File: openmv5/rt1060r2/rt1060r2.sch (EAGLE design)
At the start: 235 parts, among them CN1 S2B-PH-K-S(LF)(SN), IC1 LM66200DRLR, IC10 TCR2LF33,LM_CT, IC2 AP61300Z6-7, IC3 IS42S16160G-6BL, IC4 ATECC608B-MAHDA-T, IC5 IS25LP064D-JKLE-TR, IC7 MXC4005XC, IC8 MIMXRT1052DVL6B, IC9 KSZ8081RNDCA-TR, J1 USB4105-GF-A, J2 DNP, J3 DNP, J4 DF12-36-DS, J5 USD-1040310811, J6 DNP, J7 DNP, J8 3221-10-0300-00, M1 9774030151R, M2 9774030151R, Q1 2N7002KW_R1_00001, Q2 2N7002KW_R1_00001, Q3 2N7002KW_R1_00001, Q4 2N7002KW_R1_00001, Q5 2N7002KW_R1_00001, Q6 DMG2301L-7, Q7 2N7002KW_R1_00001, U2 BQ24075RGTR, U3 LBEE5KL1DX-883, Y1 SC32S-7PF20PPM, Y2 XRCGB24M000F3M00R0, Y3 ECS-327MVATX-3-CN-TR3

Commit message: Update R2 board per all feedback so far
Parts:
- removed C111: 0.1uF, 0402:CAP_0402
- removed IC10: TCR2LF33,LM_CT, TCR2LF33_LM_CT:TCR2LF33,LM_CT
- removed L9: MAKK2016T2R2M, MAKK2016T2R2M:MAKK2016T2R2M
- removed U3: LBEE5KL1DX-883, LBEE5KL1DX-TEMP:LBEE5KL1DX-TEMP
- added C24: 0.22uF, rcl:C-EUC0201
- added C25: 4.7uF, 0402:CAP_0402
- added D11, D12, D13, D14: CPDQT5V0HE-HF, CPDQT5V0HE-HF:CPDQT5V0HE-HF
- added D15: RB521S30T5G, RB521S30T5G:RB521S30T5G
- added IC6: ATECC608B-MAHDA-T, ATECC608B-MAHDA-T:ATECC608B-MAHDA-T
- added J9: DNP, 2337019-1:2337019-1
- added L3: 100, 0402:INDUCTOR_0402
- added R60, R61, R63: 10K, 0402:RES_0402
- added R62: 2.2M, 0402:RES_0402
- added TP1, TP2: TPTP10R, testpad:TPTP10R
- added U1: BQ24075RGTR, BQ24075RGTR:BQ24075RGTR
- C1: value 4.7uF -> 1nF; device sfe:CAP0402-CAP -> 0402:CAP_0402; MPN JMK105BBJ475MV-F -> VJ0402Y102JXACW1BC
- C10, C40, C65, C81: value 4.7uF -> 22uF; device sfe:CAP0402-CAP -> SparkFun-Capacitors:22UF-0805-6.3V-20%; MPN JMK105BBJ475MV-F -> CL21A226MQQNNNE
- C101, C2, C23, C27, C3, C35, C39, C4, C41, C42, C44, C5, C57, C72, C8, C9, C92: device sfe:CAP0402-CAP -> 0402:CAP_0402
- C103, C13, C28, C31, C38, C43, C48, C59, C62, C66, C98: value 0.22uF -> 4.7uF; device rcl:C-EUC0201 -> 0402:CAP_0402; MPN GRM033R60J224ME15D -> JMK105BBJ475MV-F
- C104, C12, C17, C21, C60, C64, C67, C83, C90, C91, C93, C95: value 4.7uF -> 0.22uF; device sfe:CAP0402-CAP -> rcl:C-EUC0201; MPN JMK105BBJ475MV-F -> GRM033R60J224ME15D
- C107: value 0.22uF -> 18pF; MPN GRM033R60J224ME15D -> GRM0335C1E180JA01D
- C108: value 4.7uF -> 18pF; device sfe:CAP0402-CAP -> rcl:C-EUC0201; MPN JMK105BBJ475MV-F -> GRM0335C1E180JA01D
- C11, C15, C19, C34, C45: value 0.22uF -> 22uF; device rcl:C-EUC0201 -> SparkFun-Capacitors:22UF-0805-6.3V-20%; MPN GRM033R60J224ME15D -> CL21A226MQQNNNE
- C110: value 1nF -> 4.7uF; device sfe:CAP0402-CAP -> 0402:CAP_0402; MPN VJ0402Y102JXACW1BC -> JMK105BBJ475MV-F
- C14, C61, C73, C85, C96: value 22uF -> 0.22uF; device SparkFun-Capacitors:22UF-0805-6.3V-20% -> rcl:C-EUC0201; MPN CL21A226MQQNNNE -> GRM033R60J224ME15D
- C18, C37, C58, C6, C7: value 22uF -> 4.7uF; device SparkFun-Capacitors:22UF-0805-6.3V-20% -> 0402:CAP_0402; MPN CL21A226MQQNNNE -> JMK105BBJ475MV-F
- C20: value 1uF -> 0.22uF; device 0402:CAP_0402 -> rcl:C-EUC0201; MPN C0402C104Z4VAC -> GRM033R60J224ME15D
- C22, C74: value 0.1uF -> 22uF; device 0402:CAP_0402 -> SparkFun-Capacitors:22UF-0805-6.3V-20%; MPN C0402C104Z4VAC -> CL21A226MQQNNNE
- C29: value 22uF -> 1uF; device SparkFun-Capacitors:22UF-0805-6.3V-20% -> 0402:CAP_0402; MPN CL21A226MQQNNNE -> C0402C104Z4VAC
- C30, C33, C46: value 4.7uF -> 0.1uF; device sfe:CAP0402-CAP -> 0402:CAP_0402; MPN JMK105BBJ475MV-F -> C0402C104Z4VAC
- C36, C82, C84: value 0.1uF -> 4.7uF; MPN C0402C104Z4VAC -> JMK105BBJ475MV-F
- C47, C50, C54, C55, C56: value 0.22uF -> 0.1uF; device rcl:C-EUC0201 -> 0402:CAP_0402; MPN GRM033R60J224ME15D -> C0402C104Z4VAC
- C51: value 22uF -> 0.1uF; device SparkFun-Capacitors:22UF-0805-6.3V-20% -> 0402:CAP_0402; MPN CL21A226MQQNNNE -> C0402C104Z4VAC
- C52: value 4.7uF -> GRM0335C1H1R5BA01D; device sfe:CAP0402-CAP -> GRM0335C1H1R5BA01D:GRM0335C1H1R5BA01D; MPN JMK105BBJ475MV-F -> GRM0335C1H1R5BA01D
- C53: value 0.22uF -> DNP; device rcl:C-EUC0201 -> GRM0335C1H1R5BA01D:GRM0335C1H1R5BA01D; MPN GRM033R60J224ME15D -> GRM0335C1H1R5BA01D; POPULATE (none) -> 0
- C75, C76, C89: value 0.1uF -> 0.22uF; device 0402:CAP_0402 -> rcl:C-EUC0201; MPN C0402C104Z4VAC -> GRM033R60J224ME15D
- C77: value GRM0335C1H1R5BA01D -> 4.7uF; device GRM0335C1H1R5BA01D:GRM0335C1H1R5BA01D -> 0402:CAP_0402; MPN GRM0335C1H1R5BA01D -> JMK105BBJ475MV-F
- C78: value DNP -> 22uF; device GRM0335C1H1R5BA01D:GRM0335C1H1R5BA01D -> SparkFun-Capacitors:22UF-0805-6.3V-20%; MPN GRM0335C1H1R5BA01D -> CL21A226MQQNNNE; POPULATE 0 -> (none)
- C79: value 18pF -> 4.7uF; device rcl:C-EUC0201 -> 0402:CAP_0402; MPN GRM0335C1E180JA01D -> JMK105BBJ475MV-F
- C80: value 18pF -> 0.22uF; MPN GRM0335C1E180JA01D -> GRM033R60J224ME15D
- D3: value UHD1110-FKA-CL1A13R3Q1BBQFMF3 -> RB521S30T5G; device UHD1110-FKA-CL1A13R3Q1BBQFMF3:UHD1110-FKA-CL1A13R3Q1BBQFMF3 -> RB521S30T5G:RB521S30T5G; MPN UHD1110-FKA-CL1A13r3q1BBQFMF3 -> RB521S30T5G
- D4: value CPDQT5V0HE-HF -> RB521S30T5G; device CPDQT5V0HE-HF:CPDQT5V0HE-HF -> RB521S30T5G:RB521S30T5G; MPN CPDQT5V0HE-HF -> RB521S30T5G
- D5: value CPDQT5V0HE-HF -> UHD1110-FKA-CL1A13R3Q1BBQFMF3; device CPDQT5V0HE-HF:CPDQT5V0HE-HF -> UHD1110-FKA-CL1A13R3Q1BBQFMF3:UHD1110-FKA-CL1A13R3Q1BBQFMF3; MPN CPDQT5V0HE-HF -> UHD1110-FKA-CL1A13r3q1BBQFMF3
- IC2: value AP61300Z6-7 -> TCR2LF33,LM_CT; device AP61300Z6-7:AP61300Z6-7 -> TCR2LF33_LM_CT:TCR2LF33,LM_CT; MPN AP61300Z6-7 -> TCR2LF33,LM(CT
- IC3: value IS42S16160G-6BL -> AP61300Z6-7; device IS42S16160G-6BL:IS42S16160G-6BL -> AP61300Z6-7:AP61300Z6-7; MPN IS42S16160G-6BL -> AP61300Z6-7
- IC4: value ATECC608B-MAHDA-T -> IS42S16160G-6BL; device ATECC608B-MAHDA-T:ATECC608B-MAHDA-T -> IS42S16160G-6BL:IS42S16160G-6BL; MPN ATECC608B-MAHDA-T -> IS42S16160G-6BL
- IC5: value IS25LP064D-JKLE-TR -> IS25LP128F-JKLE-TR; DESCRIPTION (none) -> NOR Flash 128M 2.3-3.6V 166Mhz Serial NOR Flash; MANUFACTURER_PART_NUMBER (none) -> IS25LP128F-JKLE-TR; MOUSER_PART_NUMBER (none) -> 870-5LP128F-JKLE-TR; MOUSER_PRICE-STOCK (none) -> https://www.mouser.com/ProductDetail/ISSI/IS25LP128F-JKLE-T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; MPN IS25LP064D-JKLE-TR -> IS25LP128F-JKLE-TR
- IC8: value MIMXRT1052DVL6B -> KSZ8081RNDCA-TR; device MIMXRT1052DVL6B:MIMXRT1052DVL6B -> KSZ8081RNDCA-TR:KSZ8081RNDCA-TR; MPN MIMXRT1052DVL6B -> KSZ8081RNDCA-TR
- IC9: value KSZ8081RNDCA-TR -> MIMXRT1052DVL6B; device KSZ8081RNDCA-TR:KSZ8081RNDCA-TR -> MIMXRT1052DVL6B:MIMXRT1052DVL6B; MPN KSZ8081RNDCA-TR -> MIMXRT1052DVL6B
- J2: value DNP -> USD-1040310811; device SparkFun-Connectors:CONN_08" -> 1040310811:USD-1040310811; MPN (none) -> 104031-0811; POPULATE 0 -> (none)
- J3: value DNP -> DF12-36-DS; device SparkFun-Connectors:CONN_08" -> DF12-36-DS:DF12-36-DS; MPN (none) -> DF12NB(3.0)-36DS-0.5V(51); POPULATE 0 -> (none)
- J4: value DF12-36-DS -> DNP; device DF12-36-DS:DF12-36-DS -> SparkFun-Connectors:CONN_08"; MPN DF12NB(3.0)-36DS-0.5V(51) -> (none); POPULATE (none) -> 0
- J5: value USD-1040310811 -> DNP; device 1040310811:USD-1040310811 -> SparkFun-Connectors:CONN_08"; MPN 104031-0811 -> (none); POPULATE (none) -> 0
- J7: device 2337019-1:2337019-1 -> SparkFun-Connectors:CONN_08"; MPN 2337019-1 -> (none)
- L4, L8: device sfe:INDUCTOR0402 -> 0402:INDUCTOR_0402
- L5: value MAKK2016T4R7M -> 3.9NH; device MAKK2016T4R7M:MAKK2016T4R7M -> SparkFun-Coils:INDUCTOR-0402-3.9NH; MPN MAKK2016T4R7M -> L-07C3N9SV6T
- L6: value 100 -> MAKK2016T2R2M; device sfe:INDUCTOR0402 -> MAKK2016T2R2M:MAKK2016T2R2M; MPN MFBM1V1005-101-R -> MAKK2016T2R2M
- L7: value 3.9NH -> MAKK2016T4R7M; device SparkFun-Coils:INDUCTOR-0402-3.9NH -> MAKK2016T4R7M:MAKK2016T4R7M; MPN L-07C3N9SV6T -> MAKK2016T4R7M
- Q1: value 2N7002KW_R1_00001 -> DMG2301L-7; device 2N7002KW_R1_00001:2N7002KW_R1_00001 -> DMG2301L-7:DMG2301L-7; MPN 2N7002KW_R1_00001 -> DMG2301L-7
- Q6: value DMG2301L-7 -> 2N7002KW_R1_00001; device DMG2301L-7:DMG2301L-7 -> 2N7002KW_R1_00001:2N7002KW_R1_00001; MPN DMG2301L-7 -> 2N7002KW_R1_00001
- R1, R5: value 1K -> 5.1K; device sfe:RESISTOR0402-RES -> 0402:RES_0402; MPN CRCW04021K00FKEDC -> RC0402JR-075K1L
- R10: value 1.1K -> 8.2K; device sfe:RESISTOR0402-RES -> 0402:RES_0402; MPN RC0402JR-071K1L -> CR0402-FX-8201GLF
- R11: value 46.4K -> 100K; device sfe:RESISTOR0402-RES -> 0402:RES_0402; MPN WR04X4642FTL -> AC0402FR-07100KL
- R12: value 8.2K -> 100K; device sfe:RESISTOR0402-RES -> 0402:RES_0402; MPN CR0402-FX-8201GLF -> AC0402FR-07100KL
- R13, R18, R34, R36, R4: device sfe:RESISTOR0402-RES -> 0402:RES_0402
- R15: value 2.7K -> 200K; device sfe:RESISTOR0402-RES -> 0402:RES_0402; MPN AC0402JR-072K7L -> CRCW0402200KFKEDC
- R16: value 2.7K -> 100K; device sfe:RESISTOR0402-RES -> 0402:RES_0402; MPN AC0402JR-072K7L -> AC0402FR-07100KL
- R17: value 2.7K -> 44.2K; device sfe:RESISTOR0402-RES -> 0402:RES_0402; MPN AC0402JR-072K7L -> AC0402FR-0744K2L
- R19, R35: value 220 -> 100K; device sfe:RESISTOR0402-RES -> 0402:RES_0402; MPN CRGCQ0402F220R -> AC0402FR-07100KL
- R2: value 200K -> 5.1K; device sfe:RESISTOR0402-RES -> 0402:RES_0402; MPN CRCW0402200KFKEDC -> RC0402JR-075K1L
- R20: value 220 -> 1K; device sfe:RESISTOR0402-RES -> 0402:RES_0402; MPN CRGCQ0402F220R -> CRCW04021K00FKEDC
- R21: value 220 -> 10K; device sfe:RESISTOR0402-RES -> 0402:RES_0402; MPN CRGCQ0402F220R -> AC0402FR-1310KL
- R22: value 100K -> 5.1K; device sfe:RESISTOR0402-RES -> 0402:RES_0402; MPN AC0402FR-07100KL -> RC0402JR-075K1L
- R23, R24, R25: value 100K -> 10K; device sfe:RESISTOR0402-RES -> 0402:RES_0402; MPN AC0402FR-07100KL -> AC0402FR-1310KL
- R26: value 1K -> 2.7K; device sfe:RESISTOR0402-RES -> 0402:RES_0402; MPN CRCW04021K00FKEDC -> AC0402JR-072K7L
- R27: value 10K -> 2.7K; device sfe:RESISTOR0402-RES -> 0402:RES_0402; MPN AC0402FR-1310KL -> AC0402JR-072K7L
- R28: value 100K -> 2.7K; device sfe:RESISTOR0402-RES -> 0402:RES_0402; MPN AC0402FR-07100KL -> AC0402JR-072K7L
- R29, R33, R37: value 10K -> 100K; device sfe:RESISTOR0402-RES -> 0402:RES_0402; MPN AC0402FR-1310KL -> AC0402FR-07100KL
- R3: value 100K -> 1M; device sfe:RESISTOR0402-RES -> 0402:RES_0402; MPN AC0402FR-07100KL -> CRCW04021M00FKEDC
- R30, R31: value 4.7K -> 100K; device sfe:RESISTOR0402-RES -> 0402:RES_0402; MPN AC0402FR-074K7L -> AC0402FR-07100KL
- R32: value 30K -> 100K; device sfe:RESISTOR0402-RES -> 0402:RES_0402; MPN 0402WGF3002TCE -> AC0402FR-07100KL
- R38: value 6.49K -> 10K; device sfe:RESISTOR0402-RES -> 0402:RES_0402; MPN CR0402-FX-6491GLF -> AC0402FR-1310KL
- R39: value 1K -> 100K; device sfe:RESISTOR0402-RES -> 0402:RES_0402; MPN CRCW04021K00FKEDC -> AC0402FR-07100KL
- R40: value 2.2M -> 10K; device sfe:RESISTOR0402-RES -> 0402:RES_0402; MPN RC0402FR-072M2L -> AC0402FR-1310KL
- R41: value 1M -> 4.7K; device sfe:RESISTOR0402-RES -> 0402:RES_0402; MPN CRCW04021M00FKEDC -> AC0402FR-074K7L
- R42: value 10K -> 4.7K; device sfe:RESISTOR0402-RES -> 0402:RES_0402; MPN AC0402FR-1310KL -> AC0402FR-074K7L
- R45, R46: value 100K -> DNP; MPN AC0402FR-07100KL -> DNP
- R48: value 100K -> 220; MPN AC0402FR-07100KL -> CRGCQ0402F220R
- R49, R51: value 100K -> 1K; MPN AC0402FR-07100KL -> CRCW04021K00FKEDC
- R50: value 100K -> 6.49K; MPN AC0402FR-07100KL -> CR0402-FX-6491GLF
- R52, R53: value 100K -> 10K; MPN AC0402FR-07100KL -> AC0402FR-1310KL
- R56, R57, R58: value 10K -> 100K; MPN AC0402FR-1310KL -> AC0402FR-07100KL
- R59: value 100K -> 30K; MPN AC0402FR-07100KL -> 0402WGF3002TCE
- R6, R7: value 5.1K -> 10K; device sfe:RESISTOR0402-RES -> 0402:RES_0402; MPN RC0402JR-075K1L -> AC0402FR-1310KL
- R8: value 44.2K -> 1.1K; device sfe:RESISTOR0402-RES -> 0402:RES_0402; MPN AC0402FR-0744K2L -> RC0402JR-071K1L
- R9: value 10K -> 46.4K; device sfe:RESISTOR0402-RES -> 0402:RES_0402; MPN AC0402FR-1310KL -> WR04X4642FTL
- U2: value BQ24075RGTR -> LBEE5KL1DX-883; device BQ24075RGTR:BQ24075RGTR -> LBEE5KL1DX-TEMP:LBEE5KL1DX-TEMP; MPN BQ24075RGTR -> LBEE5KL1DX-883
- Y1: value SC32S-7PF20PPM -> ECS-327MVATX-3-CN-TR3; device ABS07-32.768KHZ-7-T:ABS07-32.768KHZ-7-T -> ECS-327MVATX-3-CN-TR3:ECS-327MVATX-3-CN-TR3; MPN SC32S-7PF20PPM -> ECS-327MVATX-3-CN-TR3
- Y3: value ECS-327MVATX-3-CN-TR3 -> SC32S-7PF20PPM; device ECS-327MVATX-3-CN-TR3:ECS-327MVATX-3-CN-TR3 -> ABS07-32.768KHZ-7-T:ABS07-32.768KHZ-7-T; MPN ECS-327MVATX-3-CN-TR3 -> SC32S-7PF20PPM
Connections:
- removed net SBL_BOOT: R42.2, S1.COM_1, S1.COM_2, S1.COM_3
- new net JTAG_TDI_INT_UNUSED: J8.8, R45.2
- new net JTAG_TRSTB_INT_UNUSED: J8.9, R46.2
- new net PMIC_STBY_REQ: C110.2, D15.K, IC9.PMIC_STBY_REQ, R63.1
- new net SBL: D13.1, J6.2, R43.2
- new net SNVS_BAT: D4.A, TP1.TP
- new net SWITCH: D15.A, R61.1, R63.2, S1.COM_1, S1.COM_2, S1.COM_3
- new net VDD_SNVS_CPU: C86.1, D3.K, D4.K, IC9.VDD_SNVS_IN
- net ANT: now also C52.1, J9.SIGNAL, L5.2, U2.ANT; no longer C77.1, J7.SIGNAL, L7.2, U3.ANT
- net BAT: now also C5.2, U1.BAT_2, U1.BAT_3; no longer C8.2, U2.BAT_2, U2.BAT_3
- net BT_D_WAKE: now also IC9.GPIO_SD_B1_00, U2.BT_DEV_WAKE; no longer IC8.GPIO_SD_B1_00, U3.BT_DEV_WAKE
- net BT_H_WAKE: now also IC9.GPIO_AD_B0_14, R53.1, U2.BT_HOST_WAKE; no longer IC8.GPIO_AD_B0_14, R44.1, U3.BT_HOST_WAKE
- net BT_REG_ON: now also IC9.GPIO_AD_B0_08, R44.1, U2.BT_REG_ON; no longer IC8.GPIO_AD_B0_08, R37.1, U3.BT_REG_ON
- net BT_UART_CTS: now also IC9.GPIO_AD_B1_04, U2.!BT_UART_RTS_N; no longer IC8.GPIO_AD_B1_04, U3.!BT_UART_RTS_N
- net BT_UART_RTS: now also IC9.GPIO_AD_B1_05, U2.!BT_UART_CTS_N; no longer IC8.GPIO_AD_B1_05, U3.!BT_UART_CTS_N
- net BT_UART_RX: now also IC9.GPIO_B0_09, U2.BT_UART_TXD; no longer IC8.GPIO_B0_09, U3.BT_UART_TXD
- net BT_UART_TX: now also IC9.GPIO_B0_08, U2.BT_UART_RXD; no longer IC8.GPIO_B0_08, U3.BT_UART_RXD
- net CC1: now also R1.1; no longer R6.1
- net CC2: now also R2.1; no longer R7.1
- net CHG: now also R5.1, U1.!CHG; no longer R1.1, U2.!CHG
- net DCDC_LP: now also IC9.DCDC_LP_1, IC9.DCDC_LP_2, L7.2; no longer IC8.DCDC_LP_1, IC8.DCDC_LP_2, L5.2
- net DCDC_PSWITCH: now also C96.1, IC9.DCDC_PSWITCH, R59.1; no longer C62.1, IC8.DCDC_PSWITCH, R32.1
- net DCMI_CLK: now also IC9.GPIO_B1_15, J3.12; no longer IC8.GPIO_B1_15, J4.12
- net DCMI_D0: now also IC9.GPIO_AD_B1_15, J3.31; no longer IC8.GPIO_AD_B1_15, J4.31
- net DCMI_D1: now also IC9.GPIO_AD_B1_14, J3.29; no longer IC8.GPIO_AD_B1_14, J4.29
- net DCMI_D2: now also IC9.GPIO_AD_B1_13, J3.35; no longer IC8.GPIO_AD_B1_13, J4.35
- net DCMI_D3: now also IC9.GPIO_AD_B1_12, J3.28; no longer IC8.GPIO_AD_B1_12, J4.28
- net DCMI_D4: now also IC9.GPIO_AD_B1_11, J3.26; no longer IC8.GPIO_AD_B1_11, J4.26
- net DCMI_D5: now also IC9.GPIO_AD_B1_10, J3.33; no longer IC8.GPIO_AD_B1_10, J4.33
- net DCMI_D6: now also IC9.GPIO_AD_B0_05, J3.24; no longer IC8.GPIO_AD_B0_05, J4.24
- net DCMI_D7: now also IC9.GPIO_AD_B0_04, J3.22, R43.1; no longer IC8.GPIO_AD_B0_04, J4.22, S1.NO_1, S1.NO_2
- net DCMI_FSIN: now also J3.23, Q7.D, R39.1; no longer J4.23, Q5.D, R28.1
- net DCMI_HSYNC: now also IC9.GPIO_AD_B0_15, J3.18; no longer IC8.GPIO_AD_B0_15, J4.18
- net DCMI_MISO: now also IC9.GPIO_B0_01, J3.15; no longer IC8.GPIO_B0_01, J4.15
- net DCMI_MOSI: now also IC9.GPIO_B0_02, J3.17; no longer IC8.GPIO_B0_02, J4.17
- net DCMI_PCLK: now also IC9.GPIO_B1_12, J3.14; no longer IC8.GPIO_B1_12, J4.14
- net DCMI_PWDN: now also IC9.GPIO_B1_02, J3.25, R40.1; no longer IC8.GPIO_B1_02, J4.25, R29.1
- net DCMI_RST: now also IC9.GPIO_B1_01, J3.21, R38.1; no longer IC8.GPIO_B1_01, J4.21, R27.1
- net DCMI_SCL: now also IC9.GPIO_AD_B1_00, J3.32, R41.1; no longer IC8.GPIO_AD_B1_00, J4.32, R30.1
- net DCMI_SCLK: now also IC9.GPIO_B0_03, J3.13; no longer IC8.GPIO_B0_03, J4.13
- net DCMI_SDA: now also IC9.GPIO_AD_B1_01, J3.34, R42.1; no longer IC8.GPIO_AD_B1_01, J4.34, R31.1
- net DCMI_SSEL: now also IC9.GPIO_B0_00, J3.11, R37.1; no longer IC8.GPIO_B0_00, J4.11, R24.1
- net DCMI_VSYNC: now also IC9.GPIO_B1_13, J3.16; no longer IC8.GPIO_B1_13, J4.16
- net EN: now also IC3.EN, Q5.D, R16.1; no longer IC2.EN, Q1.D, R3.1
- net ETH_INT: now also IC8.INTRP, IC9.GPIO_B0_12, R49.1; no longer IC8.GPIO_B0_12, IC9.INTRP, R36.1
- net ETH_LED: now also IC8.LED0_/_ANEN_SPEED, R48.1; no longer IC9.LED0_/_ANEN_SPEED, R35.1
- net ETH_MDC: now also IC8.MDC, IC9.GPIO_EMC_40; no longer IC8.GPIO_EMC_40, IC9.MDC
- net ETH_MDIO: now also IC8.MDIO, IC9.GPIO_EMC_41, R51.1; no longer IC8.GPIO_EMC_41, IC9.MDIO, R39.1
- net ETH_RST: now also C42.2, IC8.RST#, IC9.GPIO_B0_13, R47.1; no longer C65.2, IC8.GPIO_B0_13, IC9.RST#, R34.1
- net ETH_RXD0: now also IC8.RXD0, IC9.GPIO_B1_04; no longer IC8.GPIO_B1_04, IC9.RXD0
- net ETH_RXD1: now also IC8.RXD1, IC9.GPIO_B1_05; no longer IC8.GPIO_B1_05, IC9.RXD1
- net ETH_RXDV: now also IC8.CRS_DV/_PHYAD[1:0], IC9.GPIO_B1_06; no longer IC8.GPIO_B1_06, IC9.CRS_DV/_PHYAD[1:0]
- net ETH_RXERR: now also IC8.RXER, IC9.GPIO_B1_11; no longer IC8.GPIO_B1_11, IC9.RXER
- net ETH_TXCLK: now also IC8.XI, IC9.GPIO_B1_10; no longer IC8.GPIO_B1_10, IC9.XI
- net ETH_TXD0: now also IC8.TXD0, IC9.GPIO_B1_07; no longer IC8.GPIO_B1_07, IC9.TXD0
- net ETH_TXD1: now also IC8.TXD1, IC9.GPIO_B1_08; no longer IC8.GPIO_B1_08, IC9.TXD1
- net ETH_TXEN: now also IC8.TXEN, IC9.GPIO_B1_09; no longer IC8.GPIO_B1_09, IC9.TXEN
- net ETH_VDDA_3.3: now also C43.2, C45.1, C46.1, IC8.VDDA_3.3, L4.P$1; no longer C81.2, C82.1, C85.1, IC9.VDDA_3.3, L8.1
- net ETH_VDD_1.2: now also C44.2, C47.1, IC8.VDD_1.2; no longer C83.2, C84.1, IC9.VDD_1.2
- net FB: now also IC3.FB, R15.1, R17.2; no longer IC2.FB, R2.1, R8.2
- net FEED: now also C53.1, L5.1; no longer C78.1, L7.1
- net GND: now also C10.2, C104.2, C108.2, C11.2, C12.1, C17.2, C19.1, C21.2, C23.2, C24.1, C25.1, C28.1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; no longer C10.1, C104.1, C108.1, C11.1, C111.2, C12.2, C17.1, C19.2, C21.1, C23.1, C28.2, C33.1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
- net ILIM: now also R8.1, U1.ILIM; no longer R10.1, U2.ILIM
- net INT_I2C_INT: now also IC9.GPIO_B1_03, R28.1; no longer IC8.GPIO_B1_03, R17.1
- net INT_I2C_SCL: now also IC6.SCL, IC9.GPIO_B0_04, R26.1; no longer IC4.SCL, IC8.GPIO_B0_04, R15.1
- net INT_I2C_SDA: now also IC6.SDA, IC9.GPIO_B0_05, R27.1; no longer IC4.SDA, IC8.GPIO_B0_05, R16.1
- net ISET: now also R10.1, U1.ISET; no longer R12.1, U2.ISET
- net JTAG_TCK: now also FL5.INPUT_5, IC9.GPIO_AD_B0_07; no longer FL5.INPUT_4, IC8.GPIO_AD_B0_07
- net JTAG_TCK_INT: now also FL5.OUTPUT_5; no longer FL5.OUTPUT_4
- net JTAG_TDI: now also FL5.INPUT_3, IC9.GPIO_AD_B0_09; no longer FL5.INPUT_2, IC8.GPIO_AD_B0_09
- net JTAG_TDI_INT: now also FL5.OUTPUT_3, J6.4, R45.1; no longer FL5.OUTPUT_2, J8.8
- net JTAG_TDO: now also FL5.INPUT_4, IC9.GPIO_AD_B0_10; no longer FL5.INPUT_3, IC8.GPIO_AD_B0_10
- net JTAG_TDO_INT: now also FL5.OUTPUT_4; no longer FL5.OUTPUT_3
- net JTAG_TMS: now also FL5.INPUT_6, IC9.GPIO_AD_B0_06; no longer FL5.INPUT_5, IC8.GPIO_AD_B0_06
- net JTAG_TMS_INT: now also FL5.OUTPUT_6; no longer FL5.OUTPUT_5
- net JTAG_TRSTB: now also FL5.INPUT_1, IC9.GPIO_AD_B0_11; no longer FL5.INPUT_6, IC8.GPIO_AD_B0_11
- net JTAG_TRSTB_INT: now also FL5.OUTPUT_1, J6.3, R46.1; no longer FL5.OUTPUT_6, J8.9
- net LED_B: now also IC9.GPIO_B1_14, R20.1, R23.1; no longer IC8.GPIO_B1_14, R19.1, R56.1
- net LED_B_INT: now also D5.BLUE, R20.2; no longer D3.BLUE, R19.2
- net LED_CHG: now also R5.2; no longer R1.2
- net LED_G: now also IC9.GPIO_B0_11, R21.1, R24.1; no longer IC8.GPIO_B0_11, R20.1, R57.1
- net LED_G_INT: now also D5.GREEN, R21.2; no longer D3.GREEN, R20.2
- net LED_PGOOD: now also R6.2; no longer R4.2
- net LED_R: now also IC9.GPIO_B0_10, R22.1, R25.1; no longer IC8.GPIO_B0_10, R21.1, R58.1
- net LED_R_INT: now also D5.RED, R22.2; no longer D3.RED, R21.2
- net LED_ST: now also R4.2; no longer R5.2
- net LPO_IN: now also U2.LPO_IN_(32KHZ), Y1.OUTPUT; no longer U3.LPO_IN_(32KHZ), Y3.OUTPUT
- net MDI_LED: now also J5.8, R48.2; no longer J3.8, R35.2
- net MDI_RX_N: now also IC8.RXM, J5.7; no longer IC9.RXM, J3.7
- net MDI_RX_P: now also IC8.RXP, J5.6; no longer IC9.RXP, J3.6
- net MDI_TX_N: now also IC8.TXM, J5.5; no longer IC9.TXM, J3.5
- net MDI_TX_P: now also IC8.TXP, J5.4; no longer IC9.TXP, J3.4
- net NVCC_PLL: now also C101.2, C102.1, IC9.NVCC_PLL; no longer C104.2, C107.1, IC8.NVCC_PLL
- net ONOFF: now also IC9.ONOFF, Q4.S; no longer IC8.ONOFF, Q3.S
- net ON_BATTERY: now also IC9.GPIO_SD_B1_04, Q2.S, R12.1; no longer IC8.GPIO_SD_B1_04, Q7.S, R59.1
- net P0_MOSI: now also FL3.INPUT_1, IC9.GPIO_AD_B0_01; no longer FL2.INPUT_1, IC8.GPIO_AD_B0_01
- net P0_MOSI_INT: now also FL3.OUTPUT_1, J4.8; no longer FL2.OUTPUT_1, J2.8
- net P10_PWM: now also Q6.D, R36.1; no longer Q4.D, R26.1
- net P10_PWM_INT: now also J7.6; no longer J6.6
- net P11_WAKEUP: now also Q3.D, R13.1; no longer Q2.D, R22.1
- net P11_WAKEUP_INT: now also J7.7; no longer J6.7
- net P12_RST_N: now also C109.1, FL5.INPUT_2, IC9.POR_B, R60.2; no longer C63.1, FL5.INPUT_1, IC8.POR_B, R33.2
- net P12_RST_N_EXT: now also FL5.OUTPUT_2, J7.8; no longer FL5.OUTPUT_1, J6.8
- net P1_MISO: now also FL3.INPUT_2, IC9.GPIO_AD_B0_02; no longer FL2.INPUT_2, IC8.GPIO_AD_B0_02
- net P1_MISO_INT: now also FL3.OUTPUT_2, J4.7; no longer FL2.OUTPUT_2, J2.7
- net P2_SCLK: now also FL3.INPUT_3, IC9.GPIO_AD_B0_00; no longer FL2.INPUT_3, IC8.GPIO_AD_B0_00
- net P2_SCLK_INT: now also FL3.OUTPUT_3, J4.6; no longer FL2.OUTPUT_3, J2.6
- net P3_NSS: now also FL3.INPUT_4, IC9.GPIO_AD_B0_03; no longer FL2.INPUT_4, IC8.GPIO_AD_B0_03
- net P3_NSS_INT: now also FL3.OUTPUT_4, J4.5; no longer FL2.OUTPUT_4, J2.5
- net P4_SCL: now also FL3.INPUT_5, IC9.GPIO_AD_B0_12; no longer FL2.INPUT_5, IC8.GPIO_AD_B0_12
- net P4_SCL_INT: now also FL3.OUTPUT_5, J4.4; no longer FL2.OUTPUT_5, J2.4
- net P5_SDA: now also FL3.INPUT_6, IC9.GPIO_AD_B0_13; no longer FL2.INPUT_6, IC8.GPIO_AD_B0_13
- net P5_SDA_INT: now also FL3.OUTPUT_6, J4.3; no longer FL2.OUTPUT_6, J2.3
- net P6_ADC: now also IC9.GPIO_AD_B1_03; no longer IC8.GPIO_AD_B1_03
- net P6_ADC_INT: now also J4.2; no longer J2.2
- net P7_PWM: now also IC9.GPIO_B0_06; no longer IC8.GPIO_B0_06
- net P7_PWM_INT: now also J7.3; no longer J6.3
- net P8_PWM: now also IC9.GPIO_B0_07; no longer IC8.GPIO_B0_07
- net P8_PWM_INT: now also J7.4; no longer J6.4
- net P9_PWM: now also IC9.GPIO_B1_00; no longer IC8.GPIO_B1_00
- net P9_PWM_INT: now also J7.5; no longer J6.5
- net PGOOD: now also Q2.D, R11.1, R6.1, U1.!PGOOD; no longer Q7.D, R14.1, R4.1, U2.!PGOOD
- net PMIC_ONOFF: now also D11.1, J5.3, Q4.D, R14.1; no longer D8.1, J3.3, Q3.D, R23.1
- net PMIC_ON_REQ: now also IC9.PMIC_ON_REQ, Q5.S; no longer IC8.PMIC_ON_REQ, Q1.S
- net PWM_FSIN: now also IC9.GPIO_SD_B1_01, Q6.S, Q7.S, R35.1; no longer IC8.GPIO_SD_B1_01, Q4.S, Q5.S, R25.1
- net P_FLASH_CE: now also IC9.GPIO_SD_B1_06, R19.2; no longer IC8.GPIO_SD_B1_06, R13.2
- net P_FLASH_IO0: now also IC9.GPIO_SD_B1_08; no longer IC8.GPIO_SD_B1_08
- net P_FLASH_IO1: now also IC9.GPIO_SD_B1_09; no longer IC8.GPIO_SD_B1_09
- net P_FLASH_IO2: now also IC9.GPIO_SD_B1_10; no longer IC8.GPIO_SD_B1_10
- net P_FLASH_IO3: now also IC9.GPIO_SD_B1_11; no longer IC8.GPIO_SD_B1_11
- net P_FLASH_SCK: now also IC9.GPIO_SD_B1_07; no longer IC8.GPIO_SD_B1_07
- net RAW: now also C10.1, C7.2, C8.2, D9.1, IC2.CONTROL, IC3.VIN, J5.2, R11.2, R13.2, R16.2, U1.EN2, U1.OUT_10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; no longer C1.2, C10.2, C6.1, D5.1, IC10.CONTROL, IC10.VIN, J3.2, R22.2, R23.2, R3.2, U2.EN2, U2.OUT_10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
- net REXT: now also IC8.REXT, R50.1; no longer IC9.REXT, R38.1
- net RTC_XTALI: now also C108.1, IC9.RTC_XTALI, Y3.2; no longer C80.1, IC8.RTC_XTALI, Y1.2
- net RTC_XTALO: now also C107.1, IC9.RTC_XTALO, Y3.1; no longer C79.1, IC8.RTC_XTALO, Y1.1
- net SDRAM_A0: now also IC4.A0, IC9.GPIO_EMC_09; no longer IC3.A0, IC8.GPIO_EMC_09
- net SDRAM_A1: now also IC4.A1, IC9.GPIO_EMC_10; no longer IC3.A1, IC8.GPIO_EMC_10
- net SDRAM_A10: now also IC4.A10, IC9.GPIO_EMC_23; no longer IC3.A10, IC8.GPIO_EMC_23
- net SDRAM_A11: now also IC4.A11, IC9.GPIO_EMC_19; no longer IC3.A11, IC8.GPIO_EMC_19
- net SDRAM_A12: now also IC4.A12, IC9.GPIO_EMC_20; no longer IC3.A12, IC8.GPIO_EMC_20
- net SDRAM_A2: now also IC4.A2, IC9.GPIO_EMC_11; no longer IC3.A2, IC8.GPIO_EMC_11
- net SDRAM_A3: now also IC4.A3, IC9.GPIO_EMC_12; no longer IC3.A3, IC8.GPIO_EMC_12
- net SDRAM_A4: now also IC4.A4, IC9.GPIO_EMC_13; no longer IC3.A4, IC8.GPIO_EMC_13
- net SDRAM_A5: now also IC4.A5, IC9.GPIO_EMC_14; no longer IC3.A5, IC8.GPIO_EMC_14
- net SDRAM_A6: now also IC4.A6, IC9.GPIO_EMC_15; no longer IC3.A6, IC8.GPIO_EMC_15
- net SDRAM_A7: now also IC4.A7, IC9.GPIO_EMC_16; no longer IC3.A7, IC8.GPIO_EMC_16
- net SDRAM_A8: now also IC4.A8, IC9.GPIO_EMC_17; no longer IC3.A8, IC8.GPIO_EMC_17
- net SDRAM_A9: now also IC4.A9, IC9.GPIO_EMC_18; no longer IC3.A9, IC8.GPIO_EMC_18
- net SDRAM_BA0: now also IC4.BA0, IC9.GPIO_EMC_21; no longer IC3.BA0, IC8.GPIO_EMC_21
- net SDRAM_BA1: now also IC4.BA1, IC9.GPIO_EMC_22; no longer IC3.BA1, IC8.GPIO_EMC_22
- net SDRAM_CAS: now also IC4.!CAS, IC9.GPIO_EMC_24; no longer IC3.!CAS, IC8.GPIO_EMC_24
- net SDRAM_CKE: now also IC4.CKE, IC9.GPIO_EMC_27; no longer IC3.CKE, IC8.GPIO_EMC_27
- net SDRAM_CLK: now also IC4.CLK, IC9.GPIO_EMC_26; no longer IC3.CLK, IC8.GPIO_EMC_26
- net SDRAM_CS: now also IC4.!CS, IC9.GPIO_EMC_29; no longer IC3.!CS, IC8.GPIO_EMC_29
- net SDRAM_DQ0: now also IC4.DQ0, IC9.GPIO_EMC_00; no longer IC3.DQ0, IC8.GPIO_EMC_00
- net SDRAM_DQ1: now also IC4.DQ1, IC9.GPIO_EMC_01; no longer IC3.DQ1, IC8.GPIO_EMC_01
- net SDRAM_DQ10: now also IC4.DQ10, IC9.GPIO_EMC_32; no longer IC3.DQ10, IC8.GPIO_EMC_32
- net SDRAM_DQ11: now also IC4.DQ11, IC9.GPIO_EMC_33; no longer IC3.DQ11, IC8.GPIO_EMC_33
- net SDRAM_DQ12: now also IC4.DQ12, IC9.GPIO_EMC_34; no longer IC3.DQ12, IC8.GPIO_EMC_34
- net SDRAM_DQ13: now also IC4.DQ13, IC9.GPIO_EMC_35; no longer IC3.DQ13, IC8.GPIO_EMC_35
- net SDRAM_DQ14: now also IC4.DQ14, IC9.GPIO_EMC_36; no longer IC3.DQ14, IC8.GPIO_EMC_36
- net SDRAM_DQ15: now also IC4.DQ15, IC9.GPIO_EMC_37; no longer IC3.DQ15, IC8.GPIO_EMC_37
- net SDRAM_DQ2: now also IC4.DQ2, IC9.GPIO_EMC_02; no longer IC3.DQ2, IC8.GPIO_EMC_02
- net SDRAM_DQ3: now also IC4.DQ3, IC9.GPIO_EMC_03; no longer IC3.DQ3, IC8.GPIO_EMC_03
- net SDRAM_DQ4: now also IC4.DQ4, IC9.GPIO_EMC_04; no longer IC3.DQ4, IC8.GPIO_EMC_04
- net SDRAM_DQ5: now also IC4.DQ5, IC9.GPIO_EMC_05; no longer IC3.DQ5, IC8.GPIO_EMC_05
- net SDRAM_DQ6: now also IC4.DQ6, IC9.GPIO_EMC_06; no longer IC3.DQ6, IC8.GPIO_EMC_06
- net SDRAM_DQ7: now also IC4.DQ7, IC9.GPIO_EMC_07; no longer IC3.DQ7, IC8.GPIO_EMC_07
- net SDRAM_DQ8: now also IC4.DQ8, IC9.GPIO_EMC_30; no longer IC3.DQ8, IC8.GPIO_EMC_30
- net SDRAM_DQ9: now also IC4.DQ9, IC9.GPIO_EMC_31; no longer IC3.DQ9, IC8.GPIO_EMC_31
- net SDRAM_DQMH: now also IC4.DQMH, IC9.GPIO_EMC_38; no longer IC3.DQMH, IC8.GPIO_EMC_38
- net SDRAM_DQML: now also IC4.DQML, IC9.GPIO_EMC_08; no longer IC3.DQML, IC8.GPIO_EMC_08
- net SDRAM_RAS: now also IC4.!RAS, IC9.GPIO_EMC_25; no longer IC3.!RAS, IC8.GPIO_EMC_25
- net SDRAM_WE: now also IC4.!WE, IC9.GPIO_EMC_28; no longer IC3.!WE, IC8.GPIO_EMC_28
- net SD_CD: now also D7.1, IC9.GPIO_AD_B1_02, J2.CD, R29.1; no longer D9.1, IC8.GPIO_AD_B1_02, J5.CD, R50.1
- net SD_CLK: now also FL2.INPUT_4, IC9.GPIO_SD_B0_01; no longer FL3.INPUT_4, IC8.GPIO_SD_B0_01
- net SD_CLK_INT: now also FL2.OUTPUT_4, J2.CLK; no longer FL3.OUTPUT_4, J5.CLK
- net SD_CMD: now also FL2.INPUT_3, IC9.GPIO_SD_B0_00, R32.1; no longer FL3.INPUT_3, IC8.GPIO_SD_B0_00, R53.1
- net SD_CMD_INT: now also FL2.OUTPUT_3, J2.CMD; no longer FL3.OUTPUT_3, J5.CMD
- net SD_DAT0: now also FL2.INPUT_5, IC9.GPIO_SD_B0_02, R31.1; no longer FL3.INPUT_5, IC8.GPIO_SD_B0_02, R52.1
- net SD_DAT0_INT: now also FL2.OUTPUT_5, J2.DAT0; no longer FL3.OUTPUT_5, J5.DAT0
- net SD_DAT1: now also FL2.INPUT_6, IC9.GPIO_SD_B0_03, R30.1; no longer FL3.INPUT_6, IC8.GPIO_SD_B0_03, R51.1
- net SD_DAT1_INT: now also FL2.OUTPUT_6, J2.DAT1; no longer FL3.OUTPUT_6, J5.DAT1
- net SD_DAT2: now also FL2.INPUT_1, IC9.GPIO_SD_B0_04, R34.1; no longer FL3.INPUT_1, IC8.GPIO_SD_B0_04, R55.1
- net SD_DAT2_INT: now also FL2.OUTPUT_1, J2.DAT2; no longer FL3.OUTPUT_1, J5.DAT2
- net SD_DAT3: now also FL2.INPUT_2, IC9.GPIO_SD_B0_05, R33.1; no longer FL3.INPUT_2, IC8.GPIO_SD_B0_05, R54.1
- net SD_DAT3_INT: now also FL2.OUTPUT_2, J2.DAT3/CD; no longer FL3.OUTPUT_2, J5.DAT3/CD
- net SHELL_GND: now also C1.2, R3.1; no longer C110.2, R41.1
- net SR_VLX: now also L6.1, U2.SR_VLX; no longer L9.1, U3.SR_VLX
- net ST: now also R4.1; no longer R5.1
- net SW: now also IC3.SW; no longer IC2.SW
- net TMR: now also R9.1, U1.TMR; no longer R11.1, U2.TMR
- net TS: now also R7.1, U1.TS; no longer R9.1, U2.TS
- net USB_D_N: now also IC9.USB_OTG1_DN; no longer IC8.USB_OTG1_DN
- net USB_D_P: now also IC9.USB_OTG1_DP; no longer IC8.USB_OTG1_DP
- net VBUS: now also C2.2, C90.1, C92.2, IC9.USB_OTG1_VBUS; no longer C3.2, C88.1, C95.2, IC8.USB_OTG1_VBUS
- net VCC: now also C103.2, C104.1, C11.1, C12.2, C17.1, C19.2, C21.1, C23.1, C24.2, C25.2, C28.2, C33.1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; no longer C108.2, C109.1, C11.2, C111.1, C12.1, C17.2, C19.1, C21.2, C23.2, C28.1, C33.2, C36.1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
- net VCC_SOC: now also C60.1, C61.1, C62.2, C63.1, C64.1, C65.2, C68.1, C89.2, C91.2, C93.2, IC9.DCDC_SENSE, IC9.VDD_SOC_IN_1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; no longer C103.2, C34.1, C38.1, C45.1, C46.2, C47.1, C48.1, C49.2, C87.2, C98.2, IC8.DCDC_SENSE, IC8.VDD_SOC_IN_1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
- net VDDA: now also C40.1, C41.2, J3.4, L3.P$1; no longer C51.1, C52.2, J4.4, L4.1
- net VDDA_ADC_3P3: now also C72.2, C73.1, C74.2, IC9.VDDA_ADC_3P3, L8.P$1; no longer C59.1, C60.2, C61.2, IC8.VDDA_ADC_3P3, L6.1
- net VDD_HIGH_CAP: now also C98.2, C99.1, IC9.VDD_HIGH_CAP; no longer C101.2, C102.1, IC8.VDD_HIGH_CAP
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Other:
- note added: "* PIN_F11 (DCMI_D7) = BOOTMOD[0] BOOTMOD = b01 -> SBL BOOT"
- note added: "* TMS = SWDIO * TCK = SWCLK * TDO = SWO"
- note added: "* TRSTB/TDI are GPIOs."
- note added: "* The JTAG Interface is designed to connect to the SEGGER 9-Pin Cortex-M Adapter. * Note that JTAG is disabled on the RT1060 by default. Only SWD works. Given this those I/O pins are routed to the external header. A fuse must be blown to switch to JTAG which disables SWD."
- note added: "3.3V"
- note added: "3.7V-5.7V"
- note added: "5V"
- note added: "BAT_3.3V"
- note added: "BAT_GND"
- note removed: "* PIN_F11 = BOOTMOD[0] BOOTMOD = b01 -> SBL BOOT"
- note removed: "* The JTAG Interface is designed to connect to the SEGGER 9-Pin Cortex-M Adapter"

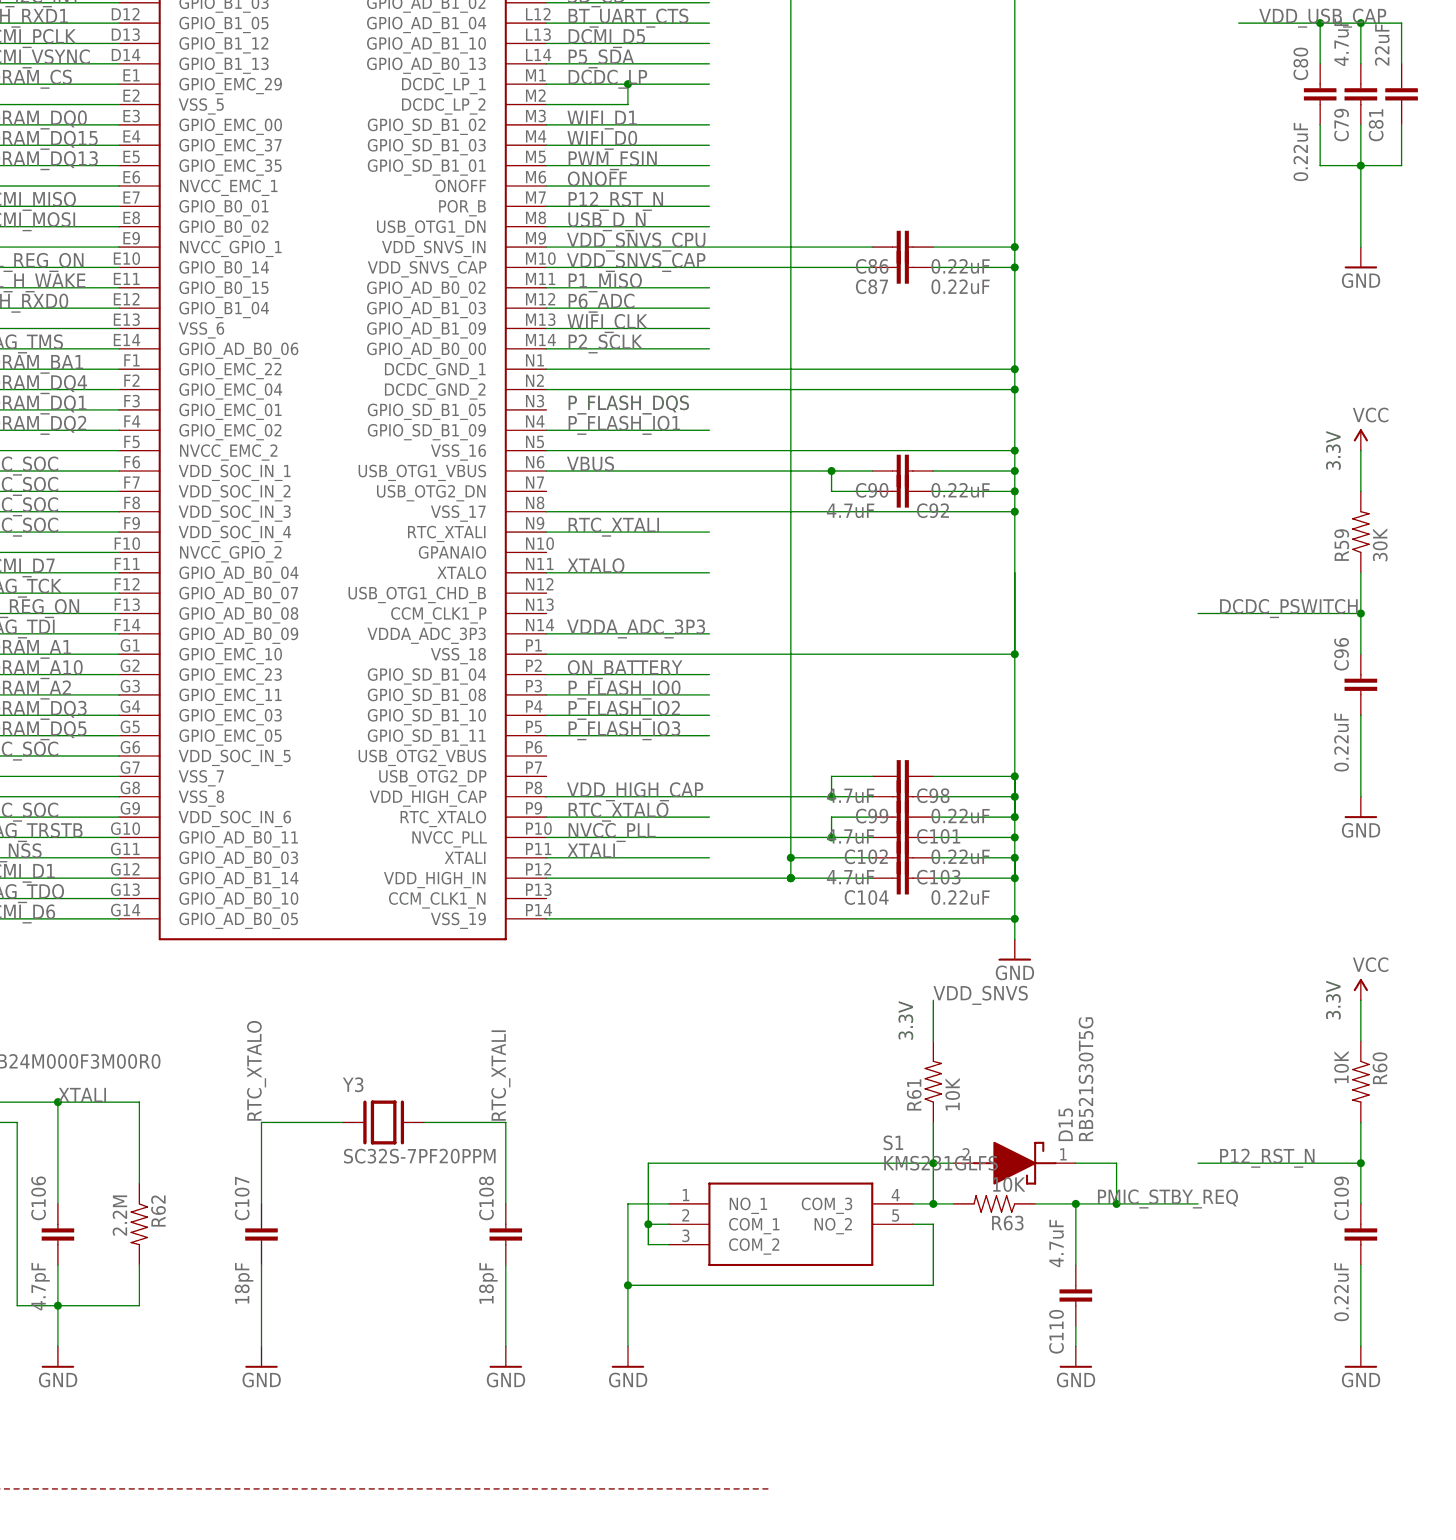
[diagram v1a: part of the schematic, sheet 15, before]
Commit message: Evaluate power off issues and fix
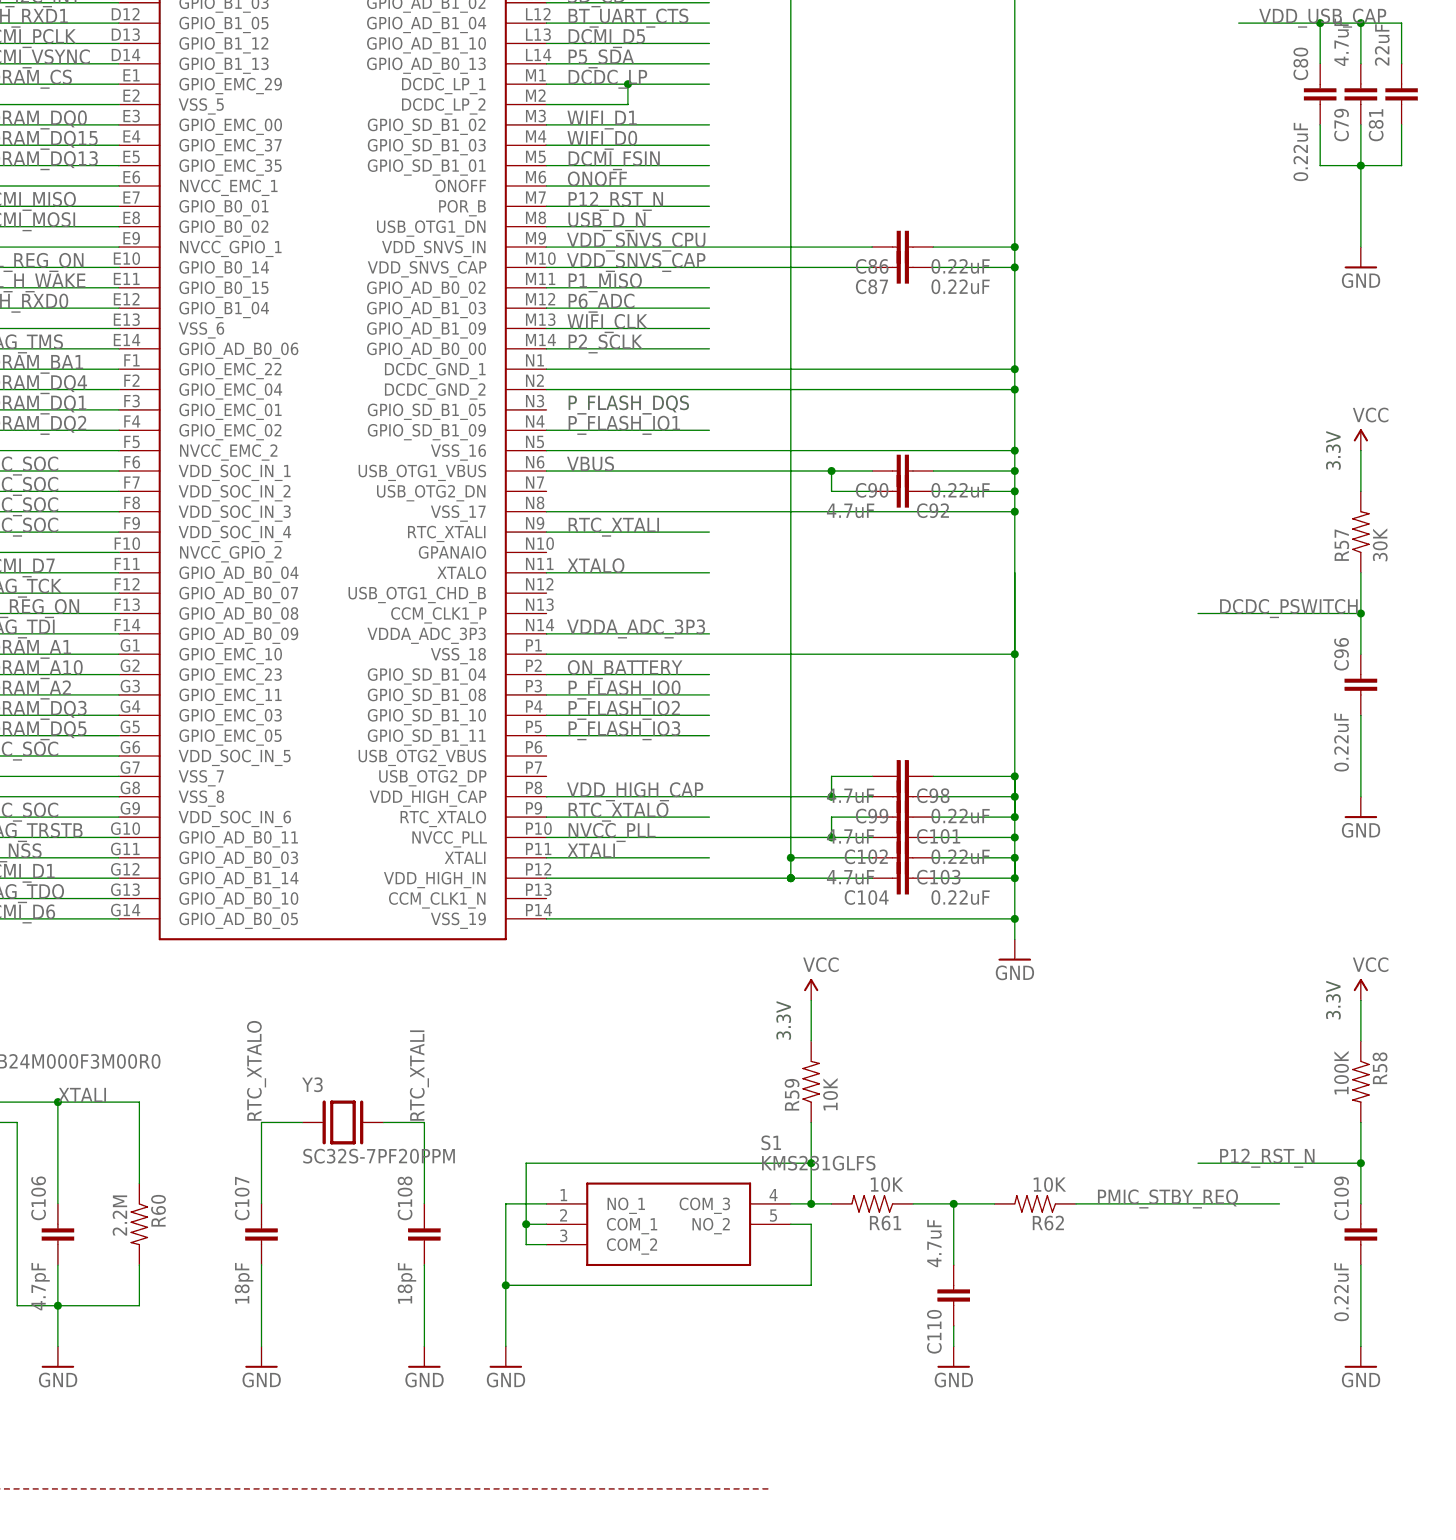
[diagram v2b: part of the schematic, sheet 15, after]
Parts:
- removed D15: RB521S30T5G, RB521S30T5G:RB521S30T5G
- removed Q6, Q7: 2N7002KW_R1_00001, 2N7002KW_R1_00001:2N7002KW_R1_00001
- removed R63: 10K, 0402:RES_0402
- R36, R51: value 1K -> 10K; MPN CRCW04021K00FKEDC -> AC0402FR-1310KL
- R39: value 100K -> 4.7K; MPN AC0402FR-07100KL -> AC0402FR-074K7L
- R40: value 10K -> 4.7K; MPN AC0402FR-1310KL -> AC0402FR-074K7L
- R41, R42: value 4.7K -> 10K; MPN AC0402FR-074K7L -> AC0402FR-1310KL
- R43, R44: value 10K -> DNP; MPN AC0402FR-1310KL -> DNP
- R45: value DNP -> 100K; MPN DNP -> AC0402FR-07100KL
- R46: value DNP -> 220; MPN DNP -> CRGCQ0402F220R
- R47: value 100K -> 1K; MPN AC0402FR-07100KL -> CRCW04021K00FKEDC
- R48: value 220 -> 6.49K; MPN CRGCQ0402F220R -> CR0402-FX-6491GLF
- R50: value 6.49K -> 10K; MPN CR0402-FX-6491GLF -> AC0402FR-1310KL
- R52, R53: value 10K -> 100K; MPN AC0402FR-1310KL -> AC0402FR-07100KL
- R57: value 100K -> 30K; MPN AC0402FR-07100KL -> 0402WGF3002TCE
- R59: value 30K -> 10K; MPN 0402WGF3002TCE -> AC0402FR-1310KL
- R60: value 10K -> 2.2M; MPN AC0402FR-1310KL -> RC0402FR-072M2L
- R62: value 2.2M -> 10K; MPN RC0402FR-072M2L -> AC0402FR-1310KL
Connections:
- removed net P10_PWM: FL4.INPUT_5, Q6.D, R36.1
- removed net PWM_FSIN: IC9.GPIO_SD_B1_01, Q6.S, Q7.S, R35.1
- new net SWITCH_OUT: C110.2, R61.1, R62.2
- net BT_H_WAKE: now also R51.1; no longer R53.1
- net BT_REG_ON: now also R42.1; no longer R44.1
- net DCDC_PSWITCH: now also R57.1; no longer R59.1
- net DCMI_D7: now also R41.1; no longer R43.1
- net DCMI_FSIN: now also FL4.INPUT_5, IC9.GPIO_SD_B1_01, R37.1; no longer Q7.D, R39.1
- net DCMI_PWDN: now also R38.1; no longer R40.1
- net DCMI_RST: now also R36.1; no longer R38.1
- net DCMI_SCL: now also R39.1; no longer R41.1
- net DCMI_SDA: now also R40.1; no longer R42.1
- net DCMI_SSEL: now also R35.1; no longer R37.1
- net ETH_INT: now also R47.1; no longer R49.1
- net ETH_LED: now also R46.1; no longer R48.1
- net ETH_MDIO: now also R49.1; no longer R51.1
- net ETH_RST: now also R45.1; no longer R47.1
- net GND: now also R36.2, R42.2, R48.2, R60.2; no longer R38.2, R44.2, R50.2, R62.2
- net JTAG_TDI_INT: now also R43.1; no longer R45.1
- net JTAG_TDI_INT_UNUSED: now also R43.2; no longer R45.2
- net JTAG_TRSTB_INT: now also R44.1; no longer R46.1
- net JTAG_TRSTB_INT_UNUSED: now also R44.2; no longer R46.2
- net MDI_LED: now also R46.2; no longer R48.2
- net P12_RST_N: now also R58.2; no longer R60.2
- net PMIC_STBY_REQ: now also R62.1; no longer C110.2, D15.K, R63.1
- net REXT: now also R48.1; no longer R50.1
- net SBL: now also R41.2; no longer R43.2
- net SWITCH: now also R59.1, R61.2; no longer D15.A, R61.1, R63.2
- net VCC: now also R38.2, R45.2, R50.2, R58.1; no longer Q6.G, Q7.G, R36.2, R41.2, R42.2, R58.2, R60.1
- net VDD_SNVS: no longer R61.2
- net WIFI_CMD: now also R56.1; no longer R58.1
- net WIFI_D0: now also R55.1; no longer R57.1
- net WIFI_D1: now also R54.1; no longer R56.1
- net WIFI_D2: now also R53.1; no longer R55.1
- net WIFI_D3: now also R52.1; no longer R54.1
- net WL_H_WAKE: now also R50.1; no longer R52.1
- net XTALI: now also R60.1; no longer R62.1
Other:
- moved on the sheet: C108, C110, Q3, Q4, R13, R14, R35, R36, R37, R38, R39, R40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
